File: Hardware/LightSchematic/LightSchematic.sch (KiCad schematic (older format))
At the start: 6 parts

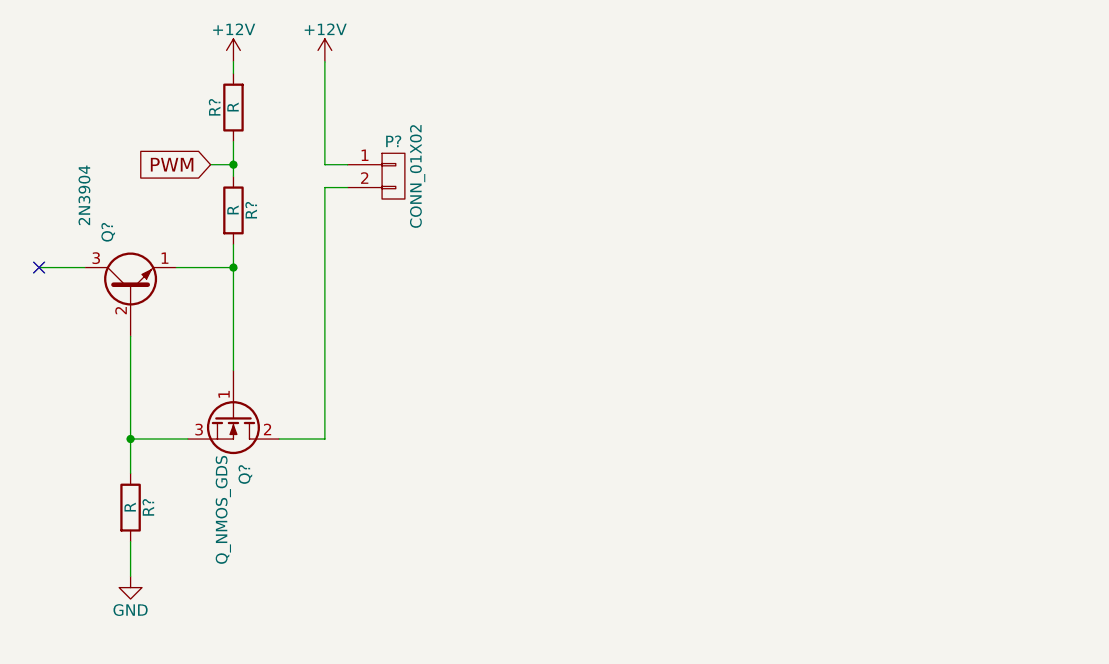
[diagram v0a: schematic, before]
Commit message: Added Super blink Updated schematic to repersent the breadboard (now 3 different light intensities Edited shine software to be a synchronized PD reader.
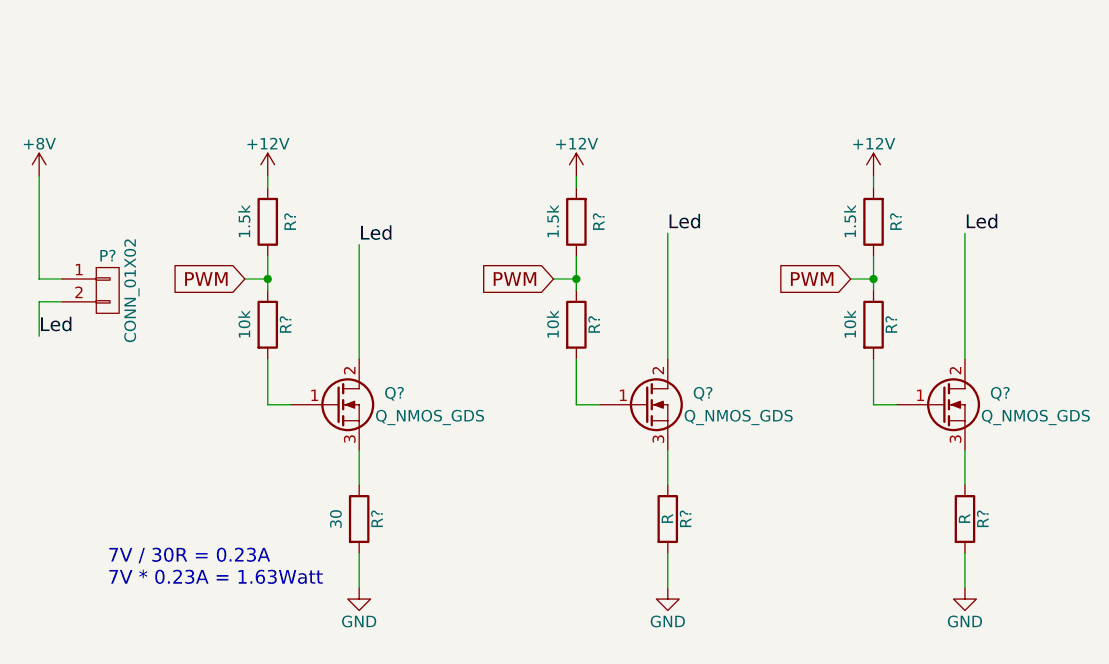
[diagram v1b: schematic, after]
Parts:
- removed Q?: 2N3904, symbol Q_NPN_EBC
- added Q? (x2): Q_NMOS_GDS, symbol Q_NMOS_GDS
- added R? (x2): R, symbol R
- added R? (x2): 10k, symbol R
- added R? (x2): 1.5k, symbol R
- R?: value R -> 30
- R?: value R -> 10k
- R?: value R -> 1.5k
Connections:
- net +12V: now also R?.2, R?.2; no longer P?.1 (P1)
- net GND: now also R?.2, R?.2
- net PWM: now also R?.1, R?.1, R?.1, R?.1
- net Led: now reaches P?.2 (P2), Q?.2 (D)
- net Led: now also Q?.2 (D), Q?.2 (D)
- new net: Q?.1 (G), R?.2 (x2)
- new net: Q?.3 (S), R?.1 (x2)
- new net +8V: P?.1 (P1)
- no-connect marks 1 -> 0
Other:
- note added: "7V / 30R = 0.23A\n7V * 0.23A = 1.63Watt"
- moved on the sheet: P?, Q?, R?

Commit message: Added all important matlab models.
I might have missed some, but atleast these are safe if my computer crahses <3.
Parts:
- added Q?: Q_NPN_BCE, symbol Q_NPN_BCE
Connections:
- wire segments 28 -> 32
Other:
- note added: "E = 1\nB = 2\nC = 3"
- moved on the sheet: R?
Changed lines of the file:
@@
 L R R?
 U 1 1 5811F559
-P 2800 2000
-F 0 "R?" V 2880 2000 50  0000 C CNN
-F 1 "10k" V 2700 2000 50  0000 C CNN
-F 2 "" V 2730 2000 50  0000 C CNN
-F 3 "" H 2800 2000 50  0000 C CNN
-	1    2800 2000
+P 2800 1750
+F 0 "R?" V 2880 1750 50  0000 C CNN
+F 1 "10k" V 2700 1750 50  0000 C CNN
+F 2 "" V 2730 1750 50  0000 C CNN
+F 3 "" H 2800 1750 50  0000 C CNN
+	1    2800 1750
 	1    0    0    -1
 $EndComp
@@
 L R R?
 U 1 1 5811F592
-P 2800 1550
-F 0 "R?" V 2700 1550 50  0000 C CNN
-F 1 "1.5k" V 2900 1550 50  0000 C CNN
-F 2 "" V 2730 1550 50  0000 C CNN
-F 3 "" H 2800 1550 50  0000 C CNN
-	1    2800 1550
+P 2800 1300
+F 0 "R?" V 2700 1300 50  0000 C CNN
+F 1 "1.5k" V 2900 1300 50  0000 C CNN
+F 2 "" V 2730 1300 50  0000 C CNN
+F 3 "" H 2800 1300 50  0000 C CNN
+	1    2800 1300
 	-1   0    0    1
 $EndComp
-Wire Wire Line
-	1800 1350 1800 1800
-Wire Wire Line
-	1800 1800 1900 1800
-Wire Wire Line
-	1900 1900 1800 1900
-Wire Wire Line
-	3200 3150 3200 3000
-Wire Wire Line
-	2800 1850 2800 1700
 $Comp
 L +12V #PWR?
 U 1 1 5811FA22
-P 2800 1350
-F 0 "#PWR?" H 2800 1200 50  0001 C CNN
-F 1 "+12V" H 2800 1490 50  0000 C CNN
-F 2 "" H 2800 1350 50  0000 C CNN
-F 3 "" H 2800 1350 50  0000 C CNN
-	1    2800 1350
-	1    0    0    -1
-$EndComp
-Wire Wire Line
-	2800 1350 2800 1400
-Text GLabel 2700 1800 0    60   Input ~ 0
+P 2800 1100
+F 0 "#PWR?" H 2800 950 50  0001 C CNN
+F 1 "+12V" H 2800 1240 50  0000 C CNN
+F 2 "" H 2800 1100 50  0000 C CNN
+F 3 "" H 2800 1100 50  0000 C CNN
+	1    2800 1100
+	1    0    0    -1
+$EndComp
+Text GLabel 2700 1550 0    60   Input ~ 0
 PWM
-Wire Wire Line
-	2700 1800 2800 1800
-Connection ~ 2800 1800
-Wire Wire Line
-	3200 2700 3200 2550
 $Comp
 L Q_NMOS_GDS Q?
@@
 	1    0    0    -1
 $EndComp
-Wire Wire Line
-	4550 3150 4550 3000
-Wire Wire Line
-	4150 2350 4250 2350
-Wire Wire Line
-	4550 2700 4550 2550
 $Comp
 L Q_NMOS_GDS Q?
@@
 	1    0    0    -1
 $EndComp
-Wire Wire Line
-	5850 3150 5850 3000
-Wire Wire Line
-	5850 2700 5850 2550
-Wire Wire Line
-	1800 1900 1800 2050
 Text Label 1800 2050 0    60   ~ 0
 Led
@@
 Text Label 5850 1600 0    60   ~ 0
 Led
-Wire Wire Line
-	5850 1600 5850 2150
-Wire Wire Line
-	4550 1600 4550 2150
-Wire Wire Line
-	3200 1650 3200 2150
-Wire Wire Line
-	2800 2150 2800 2350
-Wire Wire Line
-	2800 2350 2900 2350
-Wire Wire Line
-	4150 2350 4150 2150
-Wire Wire Line
-	5450 2150 5450 2350
-Wire Wire Line
-	5450 2350 5550 2350
 $Comp
 L +8V #PWR?
@@
 	-1   0    0    1
 $EndComp
-Wire Wire Line
-	4150 1850 4150 1700
 $Comp
 L +12V #PWR?
@@
 	1    0    0    -1
 $EndComp
-Wire Wire Line
-	4150 1350 4150 1400
 Text GLabel 4050 1800 0    60   Input ~ 0
 PWM
-Wire Wire Line
-	4050 1800 4150 1800
-Connection ~ 4150 1800
 $Comp
 L R R?
@@
 	-1   0    0    1
 $EndComp
-Wire Wire Line
-	5450 1850 5450 1700
 $Comp
 L +12V #PWR?
@@
 	1    0    0    -1
 $EndComp
-Wire Wire Line
-	5450 1350 5450 1400
 Text GLabel 5350 1800 0    60   Input ~ 0
 PWM
-Wire Wire Line
-	5350 1800 5450 1800
-Connection ~ 5450 1800
 Text Notes 2100 3150 0    60   ~ 0
 7V / 30R = 0.23A\n7V * 0.23A = 1.63Watt
+$Comp
+L Q_NPN_BCE Q?
+U 1 1 587CC680
+P 3700 2600
+F 0 "Q?" H 4000 2650 50  0000 R CNN
+F 1 "Q_NPN_BCE" H 4300 2550 50  0000 R CNN
+F 2 "" H 3900 2700 50  0000 C CNN
+F 3 "" H 3700 2600 50  0000 C CNN
+	1    3700 2600
+	1    0    0    -1
+$EndComp
+$Comp
+L GND #PWR?
+U 1 1 587CC956
+P 3800 3200
+F 0 "#PWR?" H 3800 2950 50  0001 C CNN
+F 1 "GND" H 3800 3050 50  0000 C CNN
+F 2 "" H 3800 3200 50  0000 C CNN
+F 3 "" H 3800 3200 50  0000 C CNN
+	1    3800 3200
+	1    0    0    -1
+$EndComp
+Wire Wire Line
+	3800 2800 3800 3200
+Connection ~ 3200 2600
+Wire Wire Line
+	3500 2600 3200 2600
+Connection ~ 2800 2050
+Wire Wire Line
+	3800 2050 2800 2050
+Wire Wire Line
+	3800 2400 3800 2050
+Connection ~ 5450 1800
+Wire Wire Line
+	5350 1800 5450 1800
+Wire Wire Line
+	5450 1350 5450 1400
+Wire Wire Line
+	5450 1850 5450 1700
+Connection ~ 4150 1800
+Wire Wire Line
+	4050 1800 4150 1800
+Wire Wire Line
+	4150 1350 4150 1400
+Wire Wire Line
+	4150 1850 4150 1700
+Wire Wire Line
+	5450 2350 5550 2350
+Wire Wire Line
+	5450 2150 5450 2350
+Wire Wire Line
+	4150 2350 4150 2150
+Wire Wire Line
+	2800 2350 2900 2350
+Wire Wire Line
+	2800 1900 2800 2350
+Wire Wire Line
+	3200 1650 3200 2150
+Wire Wire Line
+	4550 1600 4550 2150
+Wire Wire Line
+	5850 1600 5850 2150
+Wire Wire Line
+	1800 1900 1800 2050
+Wire Wire Line
+	5850 2700 5850 2550
+Wire Wire Line
+	5850 3150 5850 3000
+Wire Wire Line
+	4550 2700 4550 2550
+Wire Wire Line
+	4150 2350 4250 2350
+Wire Wire Line
+	4550 3150 4550 3000
+Wire Wire Line
+	3200 2700 3200 2550
+Connection ~ 2800 1550
+Wire Wire Line
+	2700 1550 2800 1550
+Wire Wire Line
+	2800 1100 2800 1150
+Wire Wire Line
+	2800 1600 2800 1450
+Wire Wire Line
+	3200 3150 3200 3000
+Wire Wire Line
+	1900 1900 1800 1900
+Wire Wire Line
+	1800 1800 1900 1800
+Wire Wire Line
+	1800 1350 1800 1800
+Text Notes 3950 3000 0    60   ~ 0
+E = 1\nB = 2\nC = 3
 $EndSCHEMATC
